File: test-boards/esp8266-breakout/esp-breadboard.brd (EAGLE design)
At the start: 20.3 x 20.3 mm, 6 parts

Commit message: cleanup to esp breadboard breakout
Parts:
- JP1: device esp:1X04 -> esp:1X04_NO_SILK
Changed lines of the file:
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@@
 <attribute name="VALUE" x="8.89" y="11.43" size="1.27" layer="27" rot="R90"/>
 </element>
-<element name="JP1" library="esp" package="1X04" value="0" x="2.54" y="13.97" smashed="yes" rot="R270">
+<element name="JP1" library="esp" package="1X04_NO_SILK" value="0" x="2.54" y="13.97" smashed="yes" rot="R270">
 <attribute name="NAME" x="1.8288" y="18.6182" size="1.27" layer="25" ratio="10" rot="R270"/>
 </element>
@@
 <wire x1="19.685" y1="19.685" x2="19.685" y2="0.635" width="1.27" layer="1"/>
 <wire x1="19.685" y1="0.635" x2="0.635" y2="0.635" width="1.27" layer="1"/>
-<wire x1="0.635" y1="0.635" x2="0.635" y2="17.78" width="1.27" layer="1"/>
+<wire x1="0.635" y1="0.635" x2="0.635" y2="17.78" width="1.016" layer="1"/>
 <wire x1="0.635" y1="17.78" x2="0.635" y2="19.685" width="1.27" layer="1"/>
 <wire x1="2.54" y1="13.97" x2="2.54" y2="17.78" width="0.6096" layer="1"/>
@@
 <wire x1="19.685" y1="19.685" x2="19.685" y2="0.635" width="1.27" layer="16"/>
 <wire x1="19.685" y1="0.635" x2="0.635" y2="0.635" width="1.27" layer="16"/>
-<wire x1="0.635" y1="0.635" x2="0.635" y2="19.685" width="1.27" layer="16"/>
+<wire x1="0.635" y1="0.635" x2="0.635" y2="19.685" width="1.016" layer="16"/>
 </signal>
 <signal name="N$1">

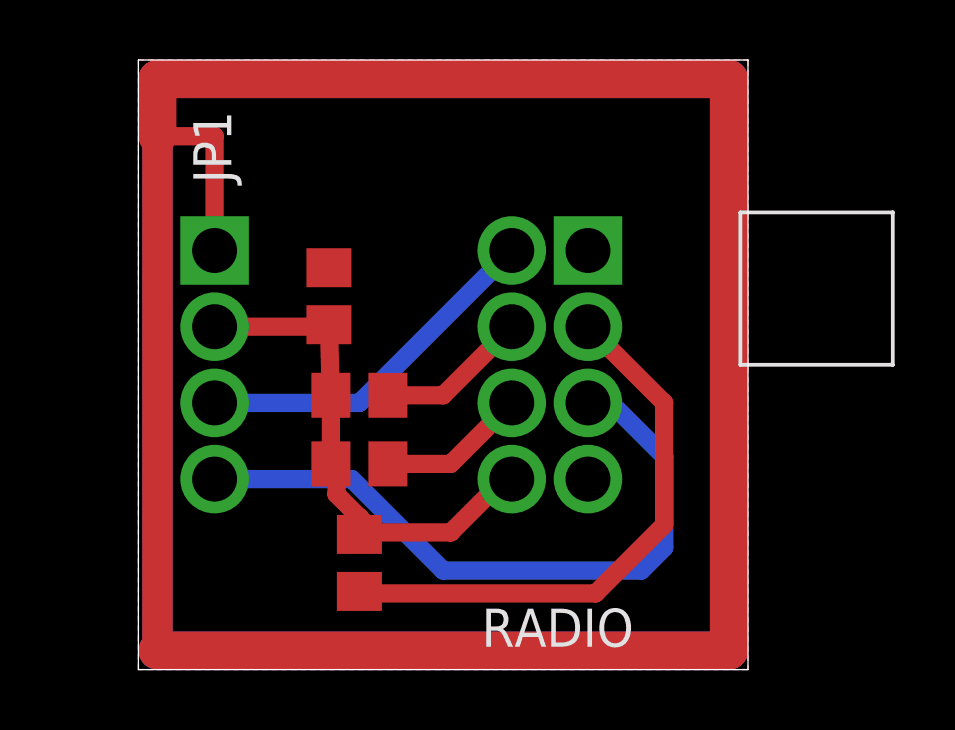
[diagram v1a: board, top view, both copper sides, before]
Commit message: ESP8266: misplaced RX and GPIO pin, switch around and resize board
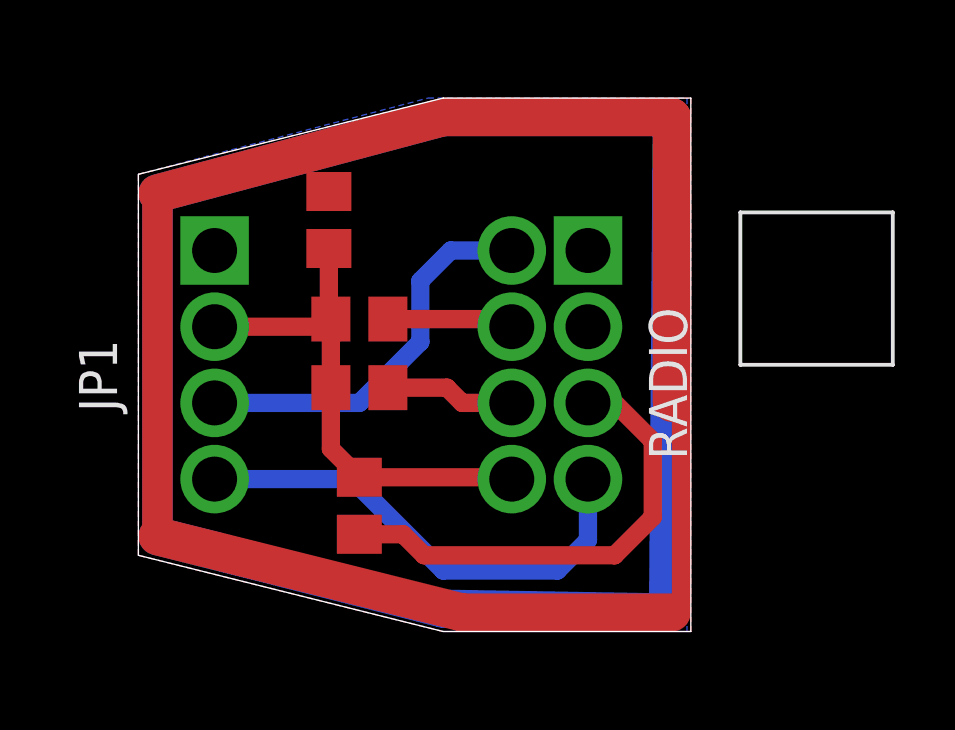
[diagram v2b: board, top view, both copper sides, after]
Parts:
- moved C1 2.54 mm to (6.35, 15.0)
- moved R3 2.54 mm to (7.37, 9.40)
- moved R1 2.54 mm to (7.37, 11.7)
- moved R2 1.91 mm to (7.37, 5.46)
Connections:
- net ESPRX: now also RADIO.4; no longer RADIO.3
- net ESPTX: now also RADIO.8; no longer RADIO.7
- net N$1: now also RADIO.3; no longer RADIO.2
- net N$2: now also RADIO.7; no longer RADIO.6
- net N$3: now also RADIO.6; no longer RADIO.5
- net VCC: now also RADIO.5; no longer RADIO.4
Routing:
- net GND: track 158.1 -> 125.0 mm
- net ESPRX: track 22.9 -> 16.2 mm
- net N$1: track 18.8 -> 15.8 mm
- net ESPTX: track 12.0 -> 13.2 mm
- net N$2: track 5.08 -> 4.24 mm
- net N$3: track 4.97 -> 4.34 mm
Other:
- board size 20.3 x 20.3 mm -> 18.4 x 17.8 mm
